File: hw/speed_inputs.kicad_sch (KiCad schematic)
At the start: 21 parts, among them U1 COMPARATOR_GENERIC

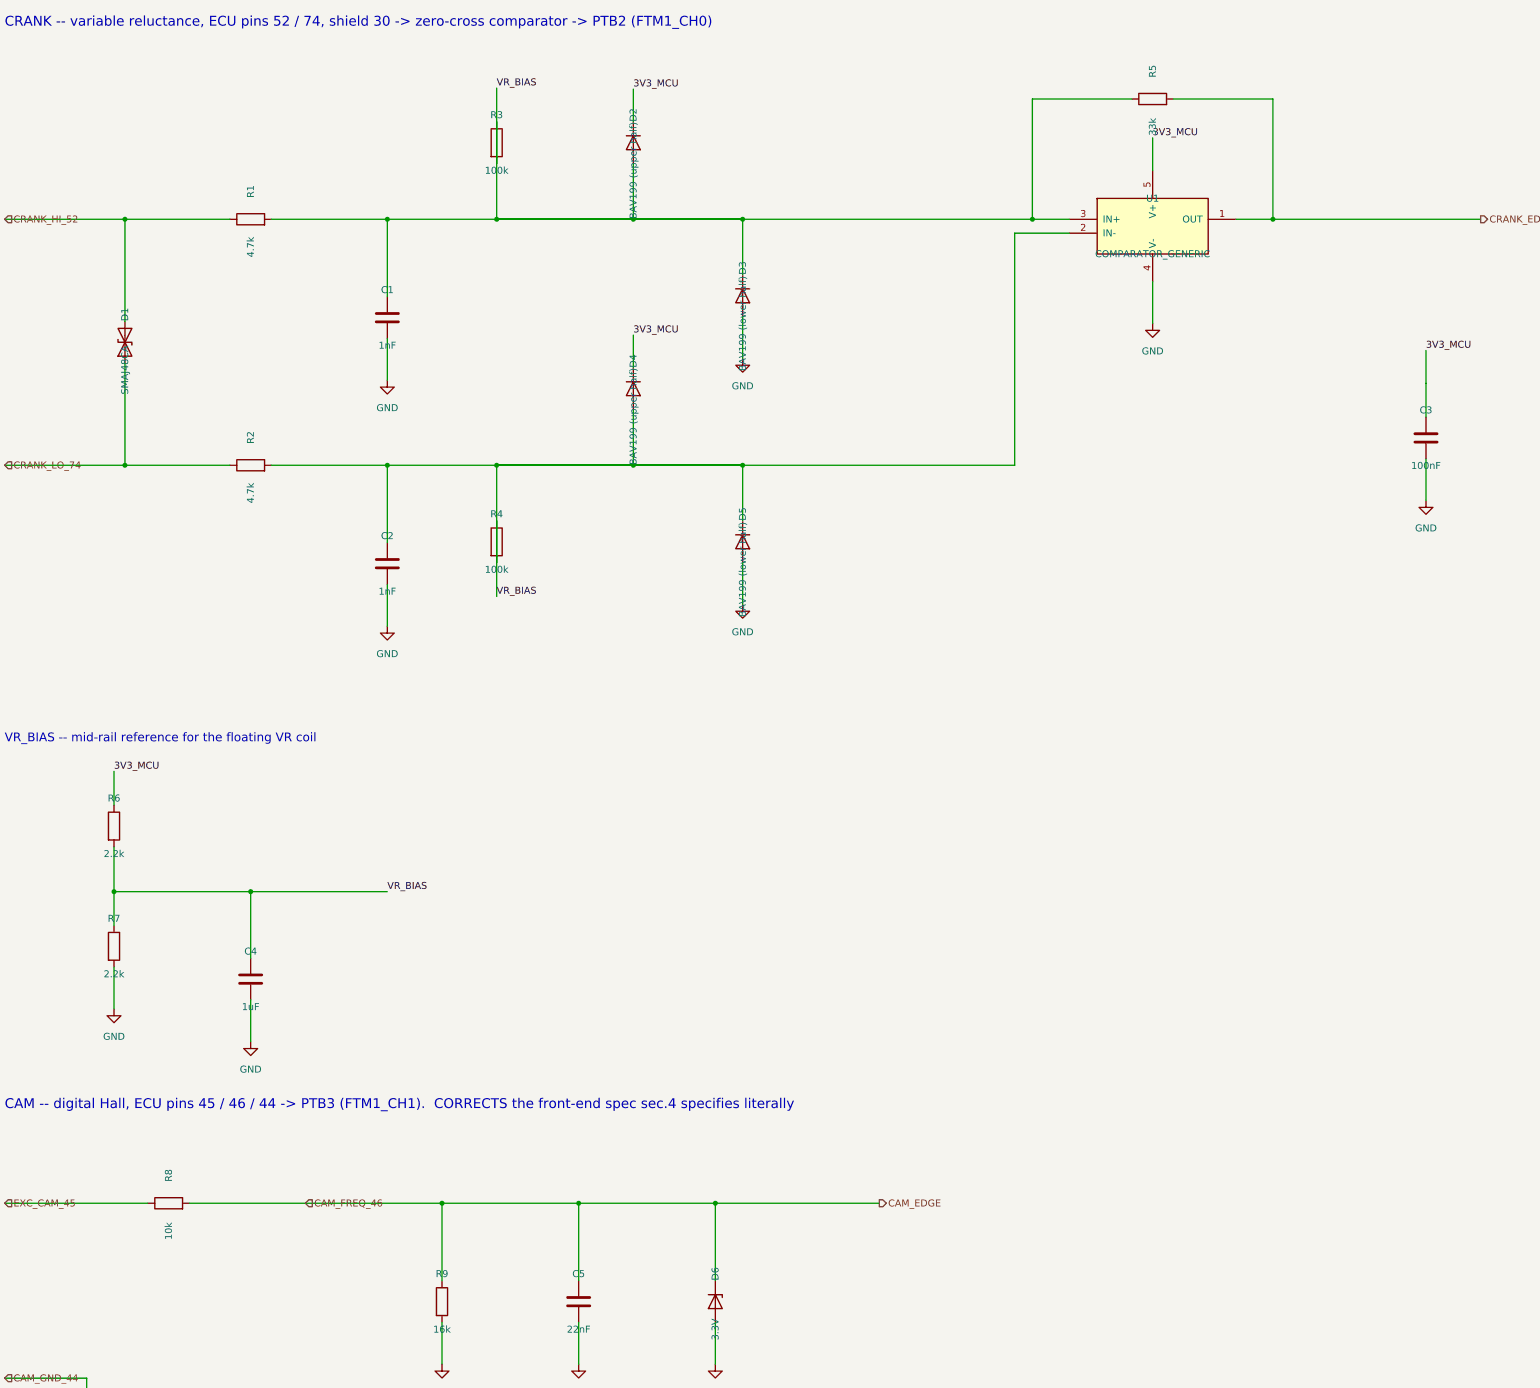
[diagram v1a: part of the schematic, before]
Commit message: Wire the root sheet: the project has a netlist for the first time
Ten sheets each passed their own netlist and the project had none. The
root sheet's ten sheet symbols carried NO hierarchical pins, so a net
name appearing on two sheets was two nets and nothing compared them --
the cross-sheet audit in the last commit was a name comparison, not a
connectivity check.

Each symbol now carries one pin per net its child exports, read OUT of
the child rather than declared in a second list that could drift: 162
pins across the ten, each with a stub and a label. Two labels with the
same name are one net, which is how 162 pins connect without routing
162 wires across a page nobody could read.

Exporting it found the other half of the same problem immediately.
kicad-cli reported annotation errors: every sheet generator allocated
R1, C1, U1 from its own counter, so ten sheets had ten parts called R1.
schlib.REF_BASE gives each sheet its own hundred -- KiCad's own
sheet-number x 100 convention, applied at generation time instead of by
a hand pass in Eeschema. 196 components, no duplicate reference.

hw/check_netlist.py is the gate, and the counterpart to sim/run_sim.py:
that one guards the component values, this one guards the connectivity.
Same rule -- an exemption is not a pass. Every single-pin net is listed
with its reason, and a net that STOPS being single-pin fails the check
until it is removed from the list. An open item that quietly closes is
as much a drift as one that quietly opens.

  196 components, every reference unique
  113 named nets carrying two or more pins
   18 named nets reaching one pin, each a recorded open item
      GND 134 pins, 3V3_MCU 27, VBAT_PROT 12 -- all spanning the project

The root sheet carries those eighteen on the page itself, grouped by
what they wait on, so a reader does not have to run a script to find
which ends are loose.

Full set plots to docs/pdf/ECU-Schematics.pdf, 11 pages.

Two rendering bugs fixed: sheet pin names and their stu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
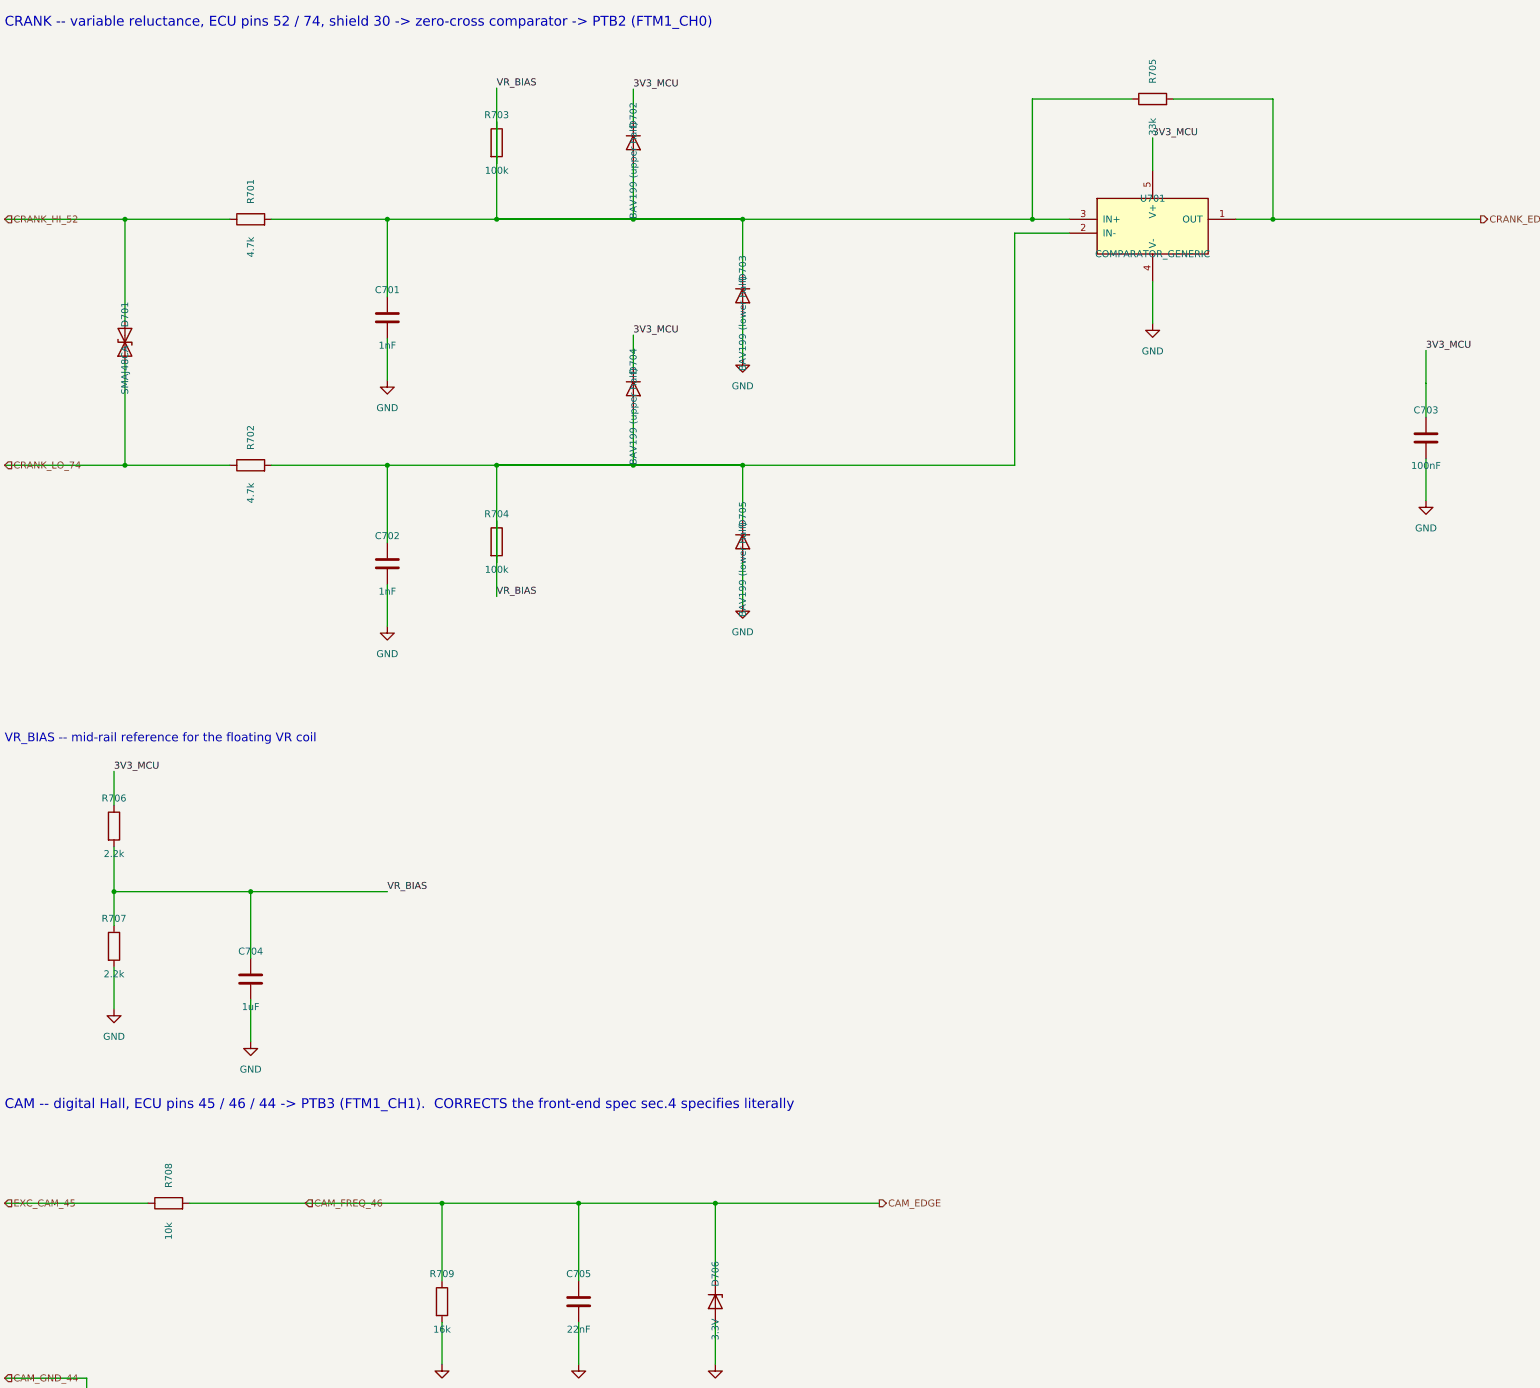
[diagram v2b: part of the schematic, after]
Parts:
- removed C1, C2: 1nF, symbol Device:C
- removed C3: 100nF, symbol Device:C
- removed C4: 1uF, symbol Device:C
- removed C5: 22nF, symbol Device:C
- removed D1: SMAJ48CA, symbol Device:D_TVS
- removed D2, D4: BAV199 (upper half), symbol Device:D
- removed D3, D5: BAV199 (lower half), symbol Device:D
- removed D6: 3.3V, symbol Device:D_Zener
- removed R1, R2: 4.7k, symbol Device:R
- removed R3, R4: 100k, symbol Device:R
- removed R5: 33k, symbol Device:R
- removed R6, R7: 2.2k, symbol Device:R
- removed R8: 10k, symbol Device:R
- removed R9: 16k, symbol Device:R
- removed U1: COMPARATOR_GENERIC, symbol ecu25kva:COMPARATOR_GENERIC
- added C701, C702: 1nF, symbol Device:C
- added C703: 100nF, symbol Device:C
- added C704: 1uF, symbol Device:C
- added C705: 22nF, symbol Device:C
- added D701: SMAJ48CA, symbol Device:D_TVS
- added D702, D704: BAV199 (upper half), symbol Device:D
- added D703, D705: BAV199 (lower half), symbol Device:D
- added D706: 3.3V, symbol Device:D_Zener
- added R701, R702: 4.7k, symbol Device:R
- added R703, R704: 100k, symbol Device:R
- added R705: 33k, symbol Device:R
- added R706, R707: 2.2k, symbol Device:R
- added R708: 10k, symbol Device:R
- added R709: 16k, symbol Device:R
- added U701: COMPARATOR_GENERIC, symbol ecu25kva:COMPARATOR_GENERIC
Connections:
- net 3V3_MCU: now also C703.1, D702.1 (K), D704.1 (K), R706.1, U701.5 (V+)
- net CAM_EDGE: now also C705.1, D706.1 (K), R708.2, R709.1
- net CRANK_EDGE: now also R705.2, U701.1 (OUT)
- net CRANK_HI_52: now also D701.2 (A2), R701.1
- net CRANK_LO_74: now also D701.1 (A1), R702.1
- net EXC_CAM_45: now also R708.1
- net GND: now also C701.2, C702.2, C703.2, C704.2, C705.2, D703.2 (A), D705.2 (A), D706.2 (A), R707.2, R709.2, U701.4 (V-)
- net VR_BIAS: now also C701.1, C702.1, C704.1, D702.2 (A), D703.1 (K), D704.2 (A), D705.1 (K), R701.2, R702.2, R703.1, R703.2, R704.1, R704.2, R705.1, R706.2, R707.1, U701.2 (IN-), U701.3 (IN+)
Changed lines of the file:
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@@
   (symbol (lib_id "ecu25kva:COMPARATOR_GENERIC") (at 250.0 71.27 0) (unit 1)
     (in_bom yes) (on_board yes) (fields_autoplaced)
-    (property "Reference" "U1" (id 0) (at 250.0 66.19 0)
+    (property "Reference" "U701" (id 0) (at 250.0 66.19 0)
       (effects (font (size 1.27 1.27)))
     )
@@
   (symbol (lib_id "power:GND") (at 250.0 89.05 0) (unit 1)
     (in_bom yes) (on_board yes) (fields_autoplaced)
-    (property "Reference" "#PWR1" (id 0) (at 250.0 83.97 0)
+    (property "Reference" "#PWR701" (id 0) (at 250.0 83.97 0)
       (effects (font (size 1.27 1.27)) hide)
     )
@@
   (symbol (lib_id "Device:D_TVS") (at 62.0 92.5 90) (unit 1)
     (in_bom yes) (on_board yes) (fields_autoplaced)
-    (property "Reference" "D1" (id 0) (at 62.0 87.42 0)
+    (property "Reference" "D701" (id 0) (at 62.0 87.42 0)
       (effects (font (size 1.27 1.27)))
     )
@@
   (symbol (lib_id "Device:R") (at 85.0 70.0 90) (unit 1)
     (in_bom yes) (on_board yes) (fields_autoplaced)
-    (property "Reference" "R1" (id 0) (at 85.0 64.92 0)
+    (property "Reference" "R701" (id 0) (at 85.0 64.92 0)
       (effects (font (size 1.27 1.27)))
     )
@@
   (symbol (lib_id "Device:C") (at 110.0 88.0 0) (unit 1)
     (in_bom yes) (on_board yes) (fields_autoplaced)
-    (property "Reference" "C1" (id 0) (at 110.0 82.92 0)
+    (property "Reference" "C701" (id 0) (at 110.0 82.92 0)
       (effects (font (size 1.27 1.27)))
     )
@@
   (symbol (lib_id "power:GND") (at 110.0 99.43 0) (unit 1)
     (in_bom yes) (on_board yes) (fields_autoplaced)
-    (property "Reference" "#PWR2" (id 0) (at 110.0 94.35000000000001 0)
+    (property "Reference" "#PWR702" (id 0) (at 110.0 94.35000000000001 0)
       (effects (font (size 1.27 1.27)) hide)
     )
@@
   (symbol (lib_id "Device:D") (at 155.0 56.0 270) (unit 1)
     (in_bom yes) (on_board yes) (fields_autoplaced)
-    (property "Reference" "D2" (id 0) (at 155.0 50.92 0)
+    (property "Reference" "D702" (id 0) (at 155.0 50.92 0)
       (effects (font (size 1.27 1.27)))
     )
@@
   (symbol (lib_id "Device:D") (at 175.0 84.0 270) (unit 1)
     (in_bom yes) (on_board yes) (fields_autoplaced)
-    (property "Reference" "D3" (id 0) (at 175.0 78.92 0)
+    (property "Reference" "D703" (id 0) (at 175.0 78.92 0)
       (effects (font (size 1.27 1.27)))
     )
@@
   (symbol (lib_id "power:GND") (at 175.0 95.43 0) (unit 1)
     (in_bom yes) (on_board yes) (fields_autoplaced)
-    (property "Reference" "#PWR3" (id 0) (at 175.0 90.35000000000001 0)
+    (property "Reference" "#PWR703" (id 0) (at 175.0 90.35000000000001 0)
       (effects (font (size 1.27 1.27)) hide)
     )
@@
   (symbol (lib_id "Device:R") (at 85.0 115.0 90) (unit 1)
     (in_bom yes) (on_board yes) (fields_autoplaced)
-    (property "Reference" "R2" (id 0) (at 85.0 109.92 0)
+    (property "Reference" "R702" (id 0) (at 85.0 109.92 0)
       (effects (font (size 1.27 1.27)))
     )
@@
   (symbol (lib_id "Device:C") (at 110.0 133.0 0) (unit 1)
     (in_bom yes) (on_board yes) (fields_autoplaced)
-    (property "Reference" "C2" (id 0) (at 110.0 127.92 0)
+    (property "Reference" "C702" (id 0) (at 110.0 127.92 0)
       (effects (font (size 1.27 1.27)))
     )
@@
   (symbol (lib_id "power:GND") (at 110.0 144.43 0) (unit 1)
     (in_bom yes) (on_board yes) (fields_autoplaced)
-    (property "Reference" "#PWR4" (id 0) (at 110.0 139.35 0)
+    (property "Reference" "#PWR704" (id 0) (at 110.0 139.35 0)
       (effects (font (size 1.27 1.27)) hide)
     )
@@
   (symbol (lib_id "Device:D") (at 155.0 101.0 270) (unit 1)
     (in_bom yes) (on_board yes) (fields_autoplaced)
-    (property "Reference" "D4" (id 0) (at 155.0 95.92 0)
+    (property "Reference" "D704" (id 0) (at 155.0 95.92 0)
       (effects (font (size 1.27 1.27)))
     )
@@
   (symbol (lib_id "Device:D") (at 175.0 129.0 270) (unit 1)
     (in_bom yes) (on_board yes) (fields_autoplaced)
-    (property "Reference" "D5" (id 0) (at 175.0 123.92 0)
+    (property "Reference" "D705" (id 0) (at 175.0 123.92 0)
       (effects (font (size 1.27 1.27)))
     )
@@
   (symbol (lib_id "power:GND") (at 175.0 140.43 0) (unit 1)
     (in_bom yes) (on_board yes) (fields_autoplaced)
-    (property "Reference" "#PWR5" (id 0) (at 175.0 135.35 0)
+    (property "Reference" "#PWR705" (id 0) (at 175.0 135.35 0)
       (effects (font (size 1.27 1.27)) hide)
     )
@@
   (symbol (lib_id "Device:R") (at 130.0 56.0 0) (unit 1)
     (in_bom yes) (on_board yes) (fields_autoplaced)
-    (property "Reference" "R3" (id 0) (at 130.0 50.92 0)
+    (property "Reference" "R703" (id 0) (at 130.0 50.92 0)
       (effects (font (size 1.27 1.27)))
     )
@@
   (symbol (lib_id "Device:R") (at 130.0 129.0 0) (unit 1)
     (in_bom yes) (on_board yes) (fields_autoplaced)
-    (property "Reference" "R4" (id 0) (at 130.0 123.92 0)
+    (property "Reference" "R704" (id 0) (at 130.0 123.92 0)
       (effects (font (size 1.27 1.27)))
     )
@@
   (symbol (lib_id "Device:R") (at 250.0 48.0 90) (unit 1)
     (in_bom yes) (on_board yes) (fields_autoplaced)
-    (property "Reference" "R5" (id 0) (at 250.0 42.92 0)
+    (property "Reference" "R705" (id 0) (at 250.0 42.92 0)
       (effects (font (size 1.27 1.27)))
     )
@@
   (symbol (lib_id "Device:C") (at 300.0 110.0 0) (unit 1)
     (in_bom yes) (on_board yes) (fields_autoplaced)
-    (property "Reference" "C3" (id 0) (at 300.0 104.92 0)
+    (property "Reference" "C703" (id 0) (at 300.0 104.92 0)
       (effects (font (size 1.27 1.27)))
     )
@@
   (symbol (lib_id "power:GND") (at 300.0 121.43 0) (unit 1)
     (in_bom yes) (on_board yes) (fields_autoplaced)
-    (property "Reference" "#PWR6" (id 0) (at 300.0 116.35000000000001 0)
+    (property "Reference" "#PWR706" (id 0) (at 300.0 116.35000000000001 0)
       (effects (font (size 1.27 1.27)) hide)
     )
@@
   (symbol (lib_id "Device:R") (at 60.0 181.0 0) (unit 1)
     (in_bom yes) (on_board yes) (fields_autoplaced)
-    (property "Reference" "R6" (id 0) (at 60.0 175.92 0)
+    (property "Reference" "R706" (id 0) (at 60.0 175.92 0)
       (effects (font (size 1.27 1.27)))
     )
@@
   (symbol (lib_id "Device:R") (at 60.0 203.0 0) (unit 1)
     (in_bom yes) (on_board yes) (fields_autoplaced)
-    (property "Reference" "R7" (id 0) (at 60.0 197.92 0)
+    (property "Reference" "R707" (id 0) (at 60.0 197.92 0)
       (effects (font (size 1.27 1.27)))
     )
@@
   (symbol (lib_id "power:GND") (at 60.0 214.43 0) (unit 1)
     (in_bom yes) (on_board yes) (fields_autoplaced)
-    (property "Reference" "#PWR7" (id 0) (at 60.0 209.35 0)
+    (property "Reference" "#PWR707" (id 0) (at 60.0 209.35 0)
       (effects (font (size 1.27 1.27)) hide)
     )
@@
   (symbol (lib_id "Device:C") (at 85.0 209.0 0) (unit 1)
     (in_bom yes) (on_board yes) (fields_autoplaced)
-    (property "Reference" "C4" (id 0) (at 85.0 203.92 0)
+    (property "Reference" "C704" (id 0) (at 85.0 203.92 0)
       (effects (font (size 1.27 1.27)))
     )
@@
   (symbol (lib_id "power:GND") (at 85.0 220.43 0) (unit 1)
     (in_bom yes) (on_board yes) (fields_autoplaced)
-    (property "Reference" "#PWR8" (id 0) (at 85.0 215.35 0)
+    (property "Reference" "#PWR708" (id 0) (at 85.0 215.35 0)
       (effects (font (size 1.27 1.27)) hide)
     )
@@
   (symbol (lib_id "power:GND") (at 345.0 182.62 0) (unit 1)
     (in_bom yes) (on_board yes) (fields_autoplaced)
-    (property "Reference" "#PWR9" (id 0) (at 345.0 177.54 0)
+    (property "Reference" "#PWR709" (id 0) (at 345.0 177.54 0)
       (effects (font (size 1.27 1.27)) hide)
     )
@@
   (symbol (lib_id "Device:R") (at 70.0 250.0 90) (unit 1)
     (in_bom yes) (on_board yes) (fields_autoplaced)
-    (property "Reference" "R8" (id 0) (at 70.0 244.92 0)
+    (property "Reference" "R708" (id 0) (at 70.0 244.92 0)
       (effects (font (size 1.27 1.27)))
     )
@@
   (symbol (lib_id "Device:R") (at 120.0 268.0 0) (unit 1)
     (in_bom yes) (on_board yes) (fields_autoplaced)
-    (property "Reference" "R9" (id 0) (at 120.0 262.92 0)
+    (property "Reference" "R709" (id 0) (at 120.0 262.92 0)
       (effects (font (size 1.27 1.27)))
     )
@@
   (symbol (lib_id "power:GND") (at 120.0 279.43 0) (unit 1)
     (in_bom yes) (on_board yes) (fields_autoplaced)
-    (property "Reference" "#PWR10" (id 0) (at 120.0 274.35 0)
+    (property "Reference" "#PWR710" (id 0) (at 120.0 274.35 0)
       (effects (font (size 1.27 1.27)) hide)
     )
@@
   (symbol (lib_id "Device:C") (at 145.0 268.0 0) (unit 1)
     (in_bom yes) (on_board yes) (fields_autoplaced)
-    (property "Reference" "C5" (id 0) (at 145.0 262.92 0)
+    (property "Reference" "C705" (id 0) (at 145.0 262.92 0)
       (effects (font (size 1.27 1.27)))
     )
@@
   (symbol (lib_id "power:GND") (at 145.0 279.43 0) (unit 1)
     (in_bom yes) (on_board yes) (fields_autoplaced)
-    (property "Reference" "#PWR11" (id 0) (at 145.0 274.35 0)
+    (property "Reference" "#PWR711" (id 0) (at 145.0 274.35 0)
       (effects (font (size 1.27 1.27)) hide)
     )
@@
   (symbol (lib_id "Device:D_Zener") (at 170.0 268.0 270) (unit 1)
     (in_bom yes) (on_board yes) (fields_autoplaced)
-    (property "Reference" "D6" (id 0) (at 170.0 262.92 0)
+    (property "Reference" "D706" (id 0) (at 170.0 262.92 0)
       (effects (font (size 1.27 1.27)))
     )
@@
   (symbol (lib_id "power:GND") (at 170.0 279.43 0) (unit 1)
     (in_bom yes) (on_board yes) (fields_autoplaced)
-    (property "Reference" "#PWR12" (id 0) (at 170.0 274.35 0)
+    (property "Reference" "#PWR712" (id 0) (at 170.0 274.35 0)
       (effects (font (size 1.27 1.27)) hide)
     )
@@
   (symbol (lib_id "power:GND") (at 55.0 289.62 0) (unit 1)
     (in_bom yes) (on_board yes) (fields_autoplaced)
-    (property "Reference" "#PWR13" (id 0) (at 55.0 284.54 0)
-      (effects (font (size 1.27 1.27)) hide)
-    )
+    (property "Reference" "#PWR713" (id 0) (at 55.0 284.54 0)
+      (effects (font (size 1.27 1.27)) hide)
+    )
